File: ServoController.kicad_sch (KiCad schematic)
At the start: 42 parts, among them J1 Conn_01x06_Male, J2 TagConnect, J3 6V-15V IN, J4 USB_C_Receptacle_USB2.0, J5 5V IN, SW1 Push Button NO 12mm SMD, SW2 Push Button NO 12mm SMD, U1 STM32F030C8T6TR, U2 EA8212FT6R, U3 AMS1117-3.3

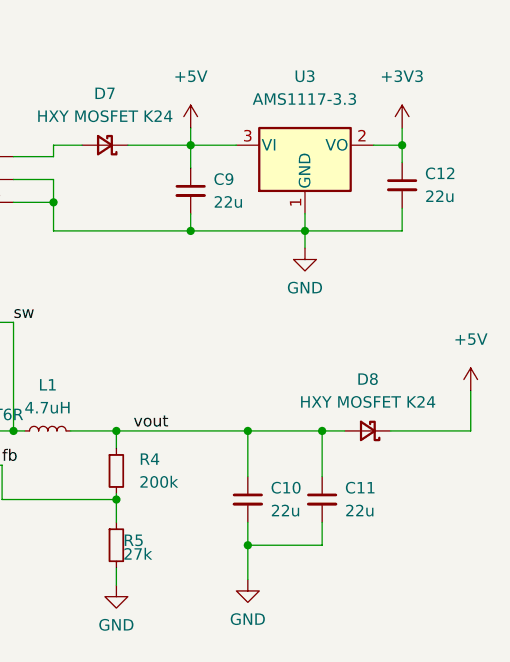
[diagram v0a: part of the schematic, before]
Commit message: Silkscreen updates
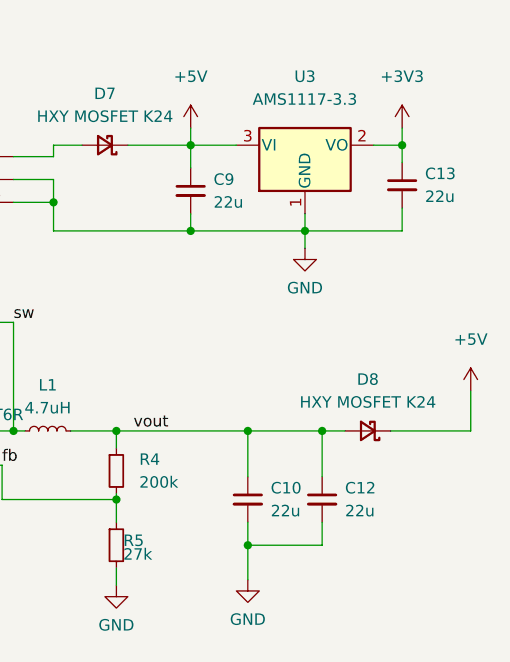
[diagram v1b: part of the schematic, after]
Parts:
- renumbered C11 to C12, C12 to C13
